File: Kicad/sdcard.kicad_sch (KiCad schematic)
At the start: 4 parts, among them J701 SD_Card

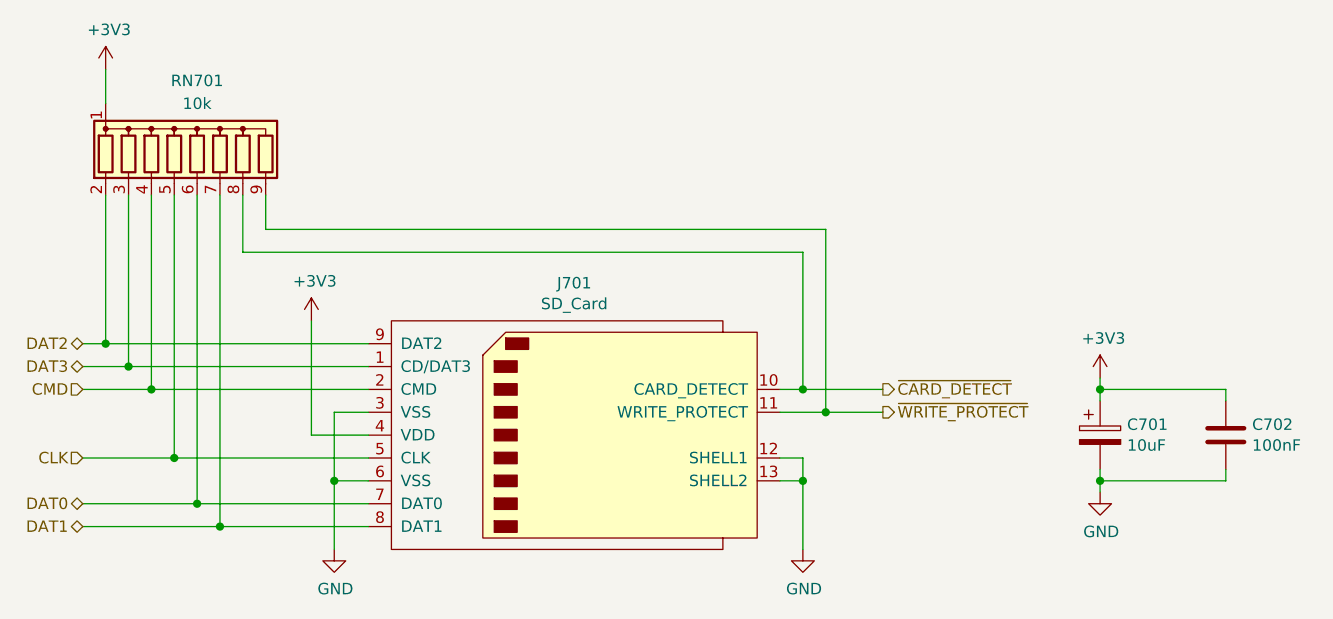
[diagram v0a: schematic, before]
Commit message: Update schematic files to Kicad 6.
Had to fix some symbols which didn't have perfect matches in K6.
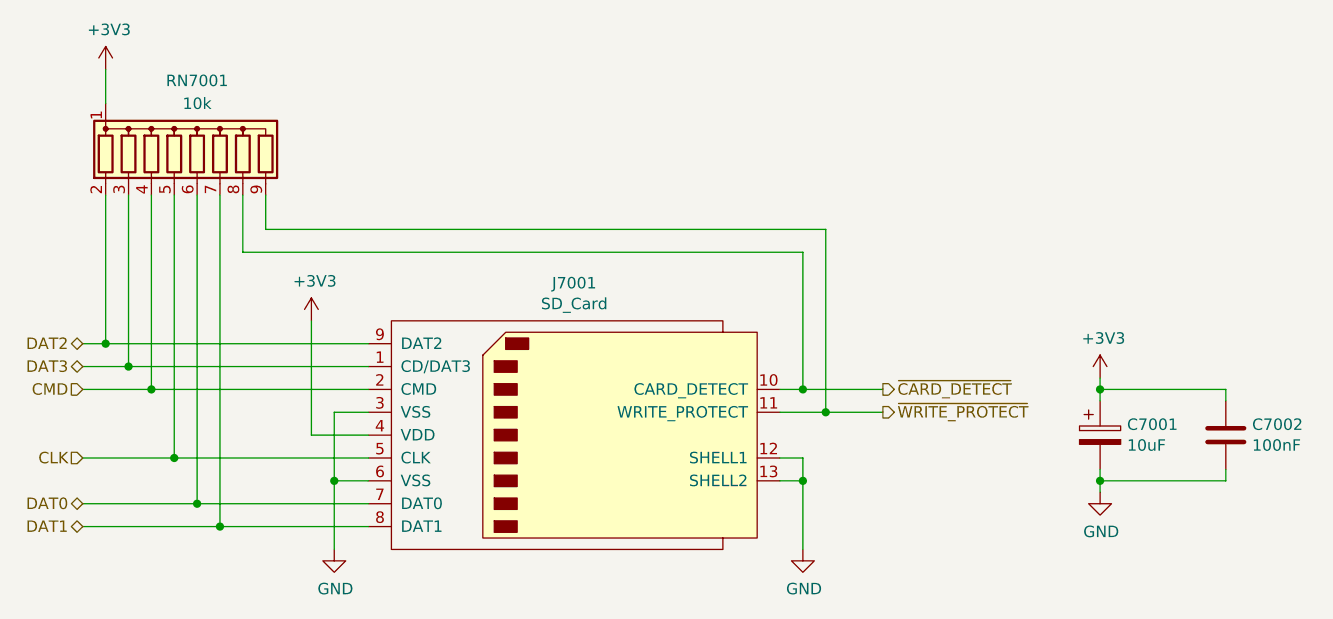
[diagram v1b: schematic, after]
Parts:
- C7001: renamed from C701; symbol Neotron-Common-Hardware-rescue:CP-Device -> Device:C_Polarized
- renumbered C702 to C7002, J701 to J7001, RN701 to RN7001
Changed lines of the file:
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@@
   (symbol (lib_id "Connector:SD_Card") (at 151.13 95.25 0) (unit 1)
     (in_bom yes) (on_board yes)
-    (property "Reference" "J701" (id 0) (at 151.13 78.359 0))
+    (property "Reference" "J7001" (id 0) (at 151.13 78.359 0))
     (property "Value" "SD_Card" (id 1) (at 151.13 80.6704 0))
     (property "Footprint" "Connector_Card:SD_Kyocera_145638009211859+" (id 2) (at 151.13 95.25 0)
@@
   (symbol (lib_id "power:+3V3") (at 121.92 82.55 0) (unit 1)
     (in_bom yes) (on_board yes)
-    (property "Reference" "#PWR0702" (id 0) (at 121.92 86.36 0)
+    (property "Reference" "#PWR07002" (id 0) (at 121.92 86.36 0)
       (effects (font (size 1.27 1.27)) hide)
     )
@@
   (symbol (lib_id "power:GND") (at 124.46 107.95 0) (unit 1)
     (in_bom yes) (on_board yes)
-    (property "Reference" "#PWR0703" (id 0) (at 124.46 114.3 0)
+    (property "Reference" "#PWR07003" (id 0) (at 124.46 114.3 0)
       (effects (font (size 1.27 1.27)) hide)
     )
@@
   (symbol (lib_id "Device:R_Network08") (at 109.22 63.5 0) (unit 1)
     (in_bom yes) (on_board yes)
-    (property "Reference" "RN701" (id 0) (at 109.22 55.88 0))
+    (property "Reference" "RN7001" (id 0) (at 109.22 55.88 0))
     (property "Value" "10k" (id 1) (at 109.22 58.42 0))
     (property "Footprint" "Resistor_THT:R_Array_SIP9" (id 2) (at 118.745 63.5 90)
@@
   (symbol (lib_id "power:+3V3") (at 99.06 54.61 0) (unit 1)
     (in_bom yes) (on_board yes)
-    (property "Reference" "#PWR0701" (id 0) (at 99.06 58.42 0)
+    (property "Reference" "#PWR07001" (id 0) (at 99.06 58.42 0)
       (effects (font (size 1.27 1.27)) hide)
     )
@@
   (symbol (lib_id "power:+3V3") (at 209.55 88.9 0) (unit 1)
     (in_bom yes) (on_board yes)
-    (property "Reference" "#PWR0705" (id 0) (at 209.55 92.71 0)
+    (property "Reference" "#PWR07005" (id 0) (at 209.55 92.71 0)
       (effects (font (size 1.27 1.27)) hide)
     )
@@
   (symbol (lib_id "power:GND") (at 209.55 101.6 0) (unit 1)
     (in_bom yes) (on_board yes)
-    (property "Reference" "#PWR0706" (id 0) (at 209.55 107.95 0)
+    (property "Reference" "#PWR07006" (id 0) (at 209.55 107.95 0)
       (effects (font (size 1.27 1.27)) hide)
     )
@@
     (pin "1")
   )
-  (symbol (lib_id "Neotron-Common-Hardware-rescue:CP-Device") (at 209.55 95.25 0) (unit 1)
-    (in_bom yes) (on_board yes)
-    (property "Reference" "C701" (id 0) (at 212.5472 94.0816 0)
+  (symbol (lib_id "Device:C_Polarized") (at 209.55 95.25 0) (unit 1)
+    (in_bom yes) (on_board yes)
+    (property "Reference" "C7001" (id 0) (at 212.5472 94.0816 0)
       (effects (font (size 1.27 1.27)) (justify left))
     )
@@
   (symbol (lib_id "Device:C") (at 223.52 95.25 0) (unit 1)
     (in_bom yes) (on_board yes)
-    (property "Reference" "C702" (id 0) (at 226.441 94.0816 0)
+    (property "Reference" "C7002" (id 0) (at 226.441 94.0816 0)
       (effects (font (size 1.27 1.27)) (justify left))
     )
@@
   (symbol (lib_id "power:GND") (at 176.53 107.95 0) (unit 1)
     (in_bom yes) (on_board yes)
-    (property "Reference" "#PWR0704" (id 0) (at 176.53 114.3 0)
-      (effects (font (size 1.27 1.27)) hide)
-    )
+    (property "Reference" "#PWR07004" (id 0) (at 176.53 114.3 0)
+      (effects (font (size 1.27 1.27)) hide)
+    )

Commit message: Imported sheets from Neotron Pico.
Standardised on +3V3 not +3.3V
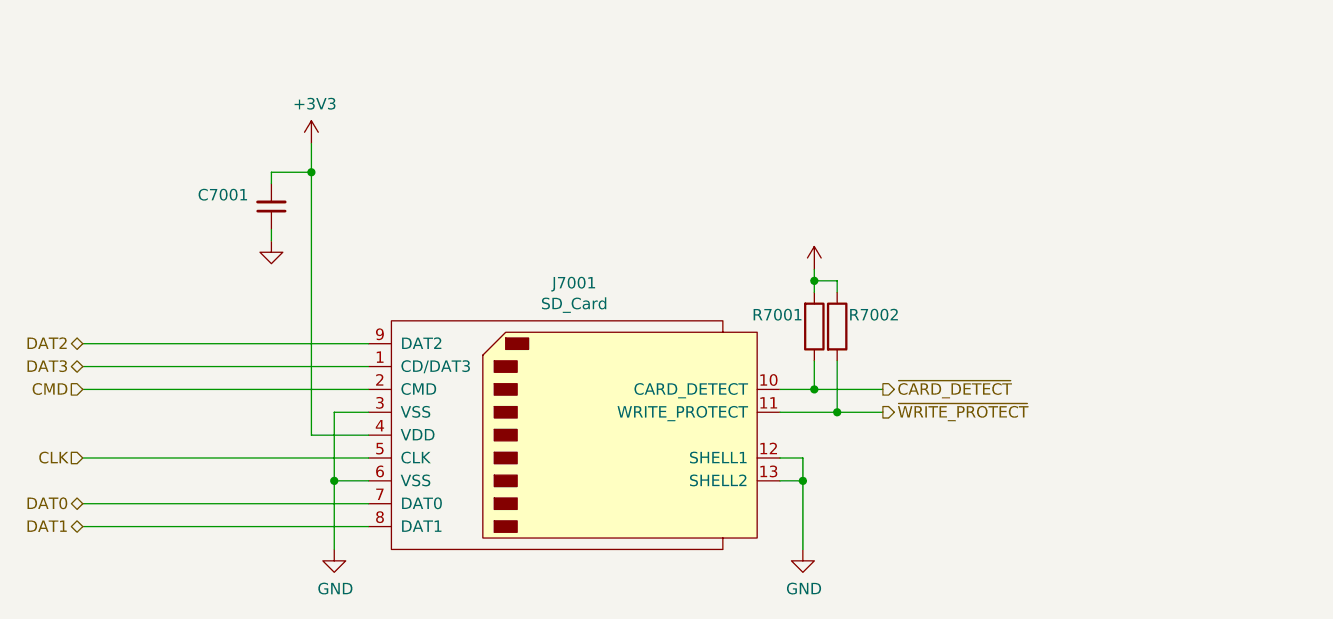
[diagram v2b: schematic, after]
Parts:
- removed C7001: 10uF, Capacitor_SMD:C_0805_2012Metric_Pad1.18x1.45mm_HandSolder, symbol Device:C_Polarized
- removed C7002: 100nF, Capacitor_SMD:C_0805_2012Metric_Pad1.18x1.45mm_HandSolder, symbol Device:C
- removed RN7001: 10k, Resistor_THT:R_Array_SIP9, symbol Device:R_Network08
- added C7001: (no value), symbol Device:C_Small
- added R7001, R7002: (no value), symbol Device:R
- J7001: Digikey 478-4059-1-ND -> 664-GSD090012SEUCT-ND; MPN 145638009211859+ -> GSD090012SEU; Manufacturer Kyocera -> Amphenol; Mouser 581-145638009211859+ -> 523-GSD090012SEU
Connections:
- net +3V3: now also C7001.2, R7001.2, R7002.1
- net GND: now also C7001.1
- net ~{CARD_DETECT}: now also R7001.1
- net ~{WRITE_PROTECT}: now also R7002.2
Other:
- company: https://neotron-compute.github.io/ -> https://neotron-compute.github.io

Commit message: Set missing footprints and update PCB
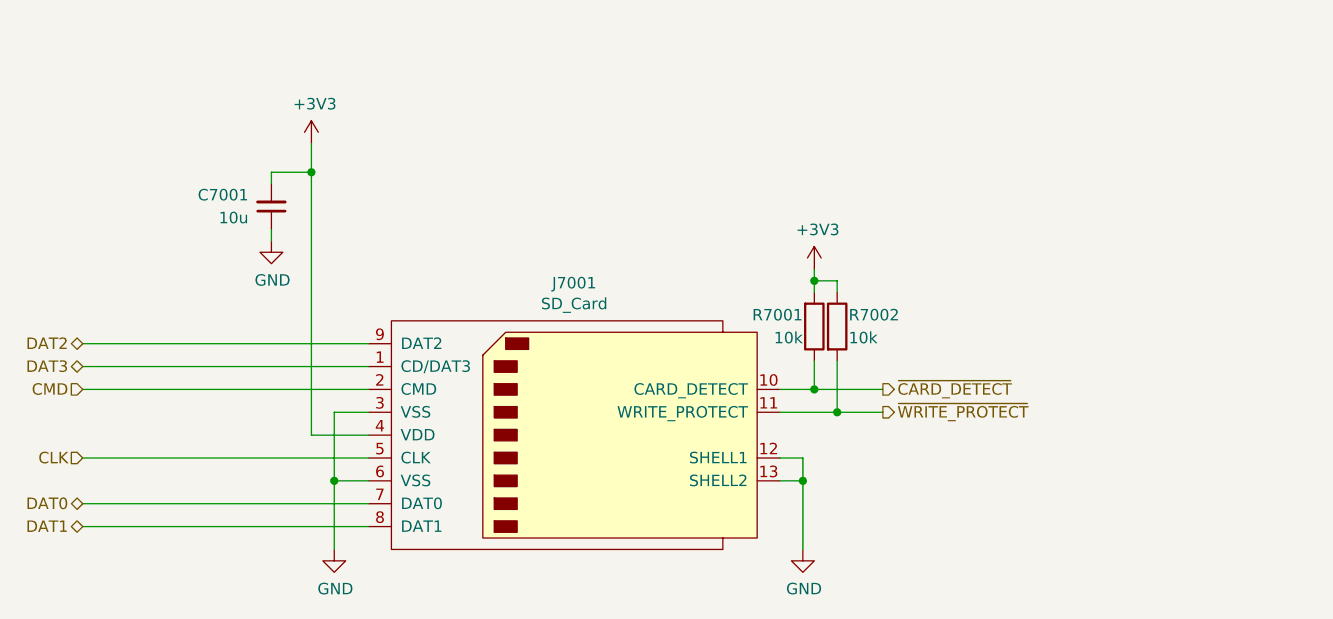
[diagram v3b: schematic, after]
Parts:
- C7001: value (none) -> 10u; footprint (none) -> Capacitor_SMD:C_0805_2012Metric_Pad1.18x1.45mm_HandSolder; JLCPCB Collection Basic -> (none); LCSC Part# C15850 -> (none); MPN CL21A106KAYNNNE -> (none); Manufacturer Samsung -> (none)
- R7001, R7002: value (none) -> 10k; footprint (none) -> Resistor_SMD:R_0805_2012Metric_Pad1.20x1.40mm_HandSolder
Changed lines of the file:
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@@
       (effects (font (size 1.27 1.27)) (justify right))
     )
-    (property "Value" "" (id 1) (at 114.935 71.12 0)
+    (property "Value" "10u" (id 1) (at 114.935 71.12 0)
       (effects (font (size 1.27 1.27)) (justify right))
     )
-    (property "Footprint" "" (id 2) (at 117.475 69.85 0)
+    (property "Footprint" "Capacitor_SMD:C_0805_2012Metric_Pad1.18x1.45mm_HandSolder" (id 2) (at 117.475 69.85 0)
       (effects (font (size 1.27 1.27)) hide)
     )
@@
       (effects (font (size 1.27 1.27)) hide)
     )
-    (property "Digikey" "~" (id 5) (at 117.475 69.85 0)
+    (property "Digikey" "" (id 5) (at 117.475 69.85 0)
       (effects (font (size 1.27 1.27)) hide)
     )
-    (property "MPN" "CL21A106KAYNNNE" (id 6) (at 117.475 69.85 0)
+    (property "MPN" "" (id 6) (at 117.475 69.85 0)
       (effects (font (size 1.27 1.27)) hide)
     )
-    (property "Manufacturer" "Samsung" (id 7) (at 117.475 69.85 0)
+    (property "Manufacturer" "" (id 7) (at 117.475 69.85 0)
       (effects (font (size 1.27 1.27)) hide)
     )
-    (property "LCSC Part#" "C15850" (id 8) (at 117.475 69.85 0)
+    (property "LCSC Part#" "" (id 8) (at 117.475 69.85 0)
       (effects (font (size 1.27 1.27)) hide)
     )
@@
       (effects (font (size 1.27 1.27)) hide)
     )
-    (property "Mouser" "~" (id 11) (at 117.475 69.85 0)
+    (property "Mouser" "" (id 11) (at 117.475 69.85 0)
       (effects (font (size 1.27 1.27)) hide)
     )
-    (property "JLCPCB Collection" "Basic" (id 12) (at 117.475 69.85 0)
+    (property "JLCPCB Collection" "" (id 12) (at 117.475 69.85 0)
       (effects (font (size 1.27 1.27)) hide)
     )
@@
       (effects (font (size 1.27 1.27)) hide)
     )
-    (property "Value" "" (id 1) (at 178.181 72.4408 0))
+    (property "Value" "+3V3" (id 1) (at 178.181 72.4408 0))
     (property "Footprint" "" (id 2) (at 177.8 76.835 0)
       (effects (font (size 1.27 1.27)) hide)
@@
       (effects (font (size 1.27 1.27)) hide)
     )
-    (property "Value" "" (id 1) (at 117.602 78.0542 0))
+    (property "Value" "GND" (id 1) (at 117.602 78.0542 0))
     (property "Footprint" "" (id 2) (at 117.475 73.66 0)
       (effects (font (size 1.27 1.27)) hide)
@@
       (effects (font (size 1.27 1.27)) (justify right))
     )
-    (property "Value" "" (id 1) (at 176.53 84.455 0)
+    (property "Value" "10k" (id 1) (at 176.53 84.455 0)
       (effects (font (size 1.27 1.27)) (justify right))
     )
-    (property "Footprint" "" (id 2) (at 176.022 83.185 90)
+    (property "Footprint" "Resistor_SMD:R_0805_2012Metric_Pad1.20x1.40mm_HandSolder" (id 2) (at 176.022 83.185 90)
       (effects (font (size 1.27 1.27)) hide)
     )
@@
       (effects (font (size 1.27 1.27)) (justify left))
     )
-    (property "Value" "" (id 1) (at 181.61 84.455 0)
+    (property "Value" "10k" (id 1) (at 181.61 84.455 0)
       (effects (font (size 1.27 1.27)) (justify left))
     )
-    (property "Footprint" "" (id 2) (at 178.562 83.185 90)
+    (property "Footprint" "Resistor_SMD:R_0805_2012Metric_Pad1.20x1.40mm_HandSolder" (id 2) (at 178.562 83.185 90)
       (effects (font (size 1.27 1.27)) hide)
     )

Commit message: Re-imported from Neotron Pico v1.1.
This time I deleted the sheets from the top level and then re-added pointing at the new files. I also reset the PCB dimensions to match the Neotron Pico.

This seems to have done a better job importing footprints.
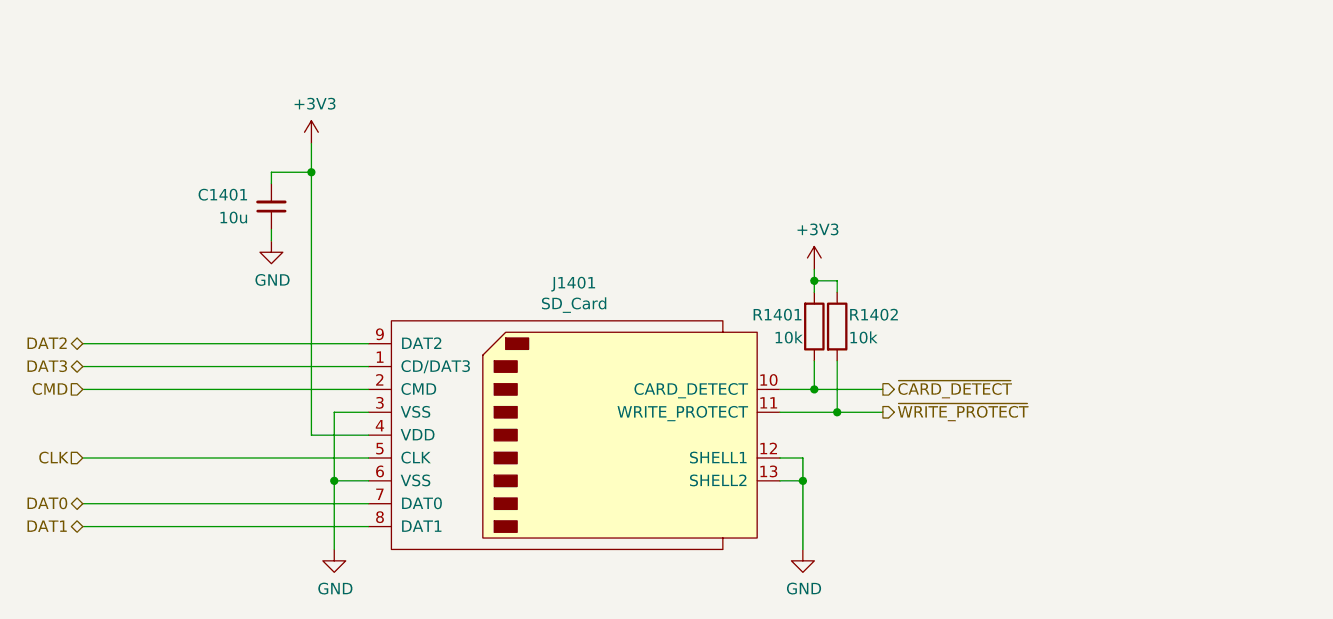
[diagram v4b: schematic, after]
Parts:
- C1401: renamed from C7001; JLCPCB Collection (none) -> Basic; LCSC Part# (none) -> C15850; MPN (none) -> CL21A106KAYNNNE; Manufacturer (none) -> Samsung
- J1401: renamed from J7001; footprint Connector_Card:SD_Kyocera_145638009211859+ -> Neotron-Common-Hardware:Amphenol_GSD090012SEU
- renumbered R7001 to R1401, R7002 to R1402
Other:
- company: https://neotron-compute.github.io -> https://neotron-compute.github.io/
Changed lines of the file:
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@@
     (title "Neotron Common Hardware - SD Card Slot")
     (date "${date}")
-    (rev "${version}")
-    (company "https://neotron-compute.github.io")
-    (comment 1 "Licensed as CC-BY-SA")
+    (rev "[Uncontrolled]")
+    (company "https://neotron-compute.github.io/")
+    (comment 1 "Licenced as CC BY-SA")
     (comment 2 "Copyright (c) The Neotron Developers, 2022")
   )
@@
   (symbol (lib_id "Connector:SD_Card") (at 151.13 95.25 0) (unit 1)
     (in_bom yes) (on_board yes)
-    (property "Reference" "J7001" (id 0) (at 151.13 78.359 0))
+    (property "Reference" "J1401" (id 0) (at 151.13 78.359 0))
     (property "Value" "SD_Card" (id 1) (at 151.13 80.6704 0))
-    (property "Footprint" "Connector_Card:SD_Kyocera_145638009211859+" (id 2) (at 151.13 95.25 0)
+    (property "Footprint" "Neotron-Common-Hardware:Amphenol_GSD090012SEU" (id 2) (at 151.13 95.25 0)
       (effects (font (size 1.27 1.27)) hide)
     )
@@
   (symbol (lib_id "power:+3V3") (at 121.92 62.865 0) (unit 1)
     (in_bom yes) (on_board yes)
-    (property "Reference" "#PWR07002" (id 0) (at 121.92 66.675 0)
+    (property "Reference" "#PWR01402" (id 0) (at 121.92 66.675 0)
       (effects (font (size 1.27 1.27)) hide)
     )
@@
   (symbol (lib_id "power:GND") (at 124.46 107.95 0) (unit 1)
     (in_bom yes) (on_board yes)
-    (property "Reference" "#PWR07003" (id 0) (at 124.46 114.3 0)
+    (property "Reference" "#PWR01403" (id 0) (at 124.46 114.3 0)
       (effects (font (size 1.27 1.27)) hide)
     )
@@
   (symbol (lib_id "power:GND") (at 176.53 107.95 0) (unit 1)
     (in_bom yes) (on_board yes)
-    (property "Reference" "#PWR07004" (id 0) (at 176.53 114.3 0)
+    (property "Reference" "#PWR01404" (id 0) (at 176.53 114.3 0)
       (effects (font (size 1.27 1.27)) hide)
     )
@@
   (symbol (lib_id "Device:C_Small") (at 117.475 69.85 0) (mirror x) (unit 1)
     (in_bom yes) (on_board yes)
-    (property "Reference" "C7001" (id 0) (at 114.935 68.58 0)
+    (property "Reference" "C1401" (id 0) (at 114.935 68.58 0)
       (effects (font (size 1.27 1.27)) (justify right))
     )
@@
       (effects (font (size 1.27 1.27)) hide)
     )
-    (property "Digikey" "" (id 5) (at 117.475 69.85 0)
-      (effects (font (size 1.27 1.27)) hide)
-    )
-    (property "MPN" "" (id 6) (at 117.475 69.85 0)
-      (effects (font (size 1.27 1.27)) hide)
-    )
-    (property "Manufacturer" "" (id 7) (at 117.475 69.85 0)
-      (effects (font (size 1.27 1.27)) hide)
-    )
-    (property "LCSC Part#" "" (id 8) (at 117.475 69.85 0)
+    (property "Digikey" "~" (id 5) (at 117.475 69.85 0)
+      (effects (font (size 1.27 1.27)) hide)
+    )
+    (property "MPN" "CL21A106KAYNNNE" (id 6) (at 117.475 69.85 0)
+      (effects (font (size 1.27 1.27)) hide)
+    )
+    (property "Manufacturer" "Samsung" (id 7) (at 117.475 69.85 0)
+      (effects (font (size 1.27 1.27)) hide)
+    )
+    (property "LCSC Part#" "C15850" (id 8) (at 117.475 69.85 0)
       (effects (font (size 1.27 1.27)) hide)
     )
@@
       (effects (font (size 1.27 1.27)) hide)
     )
-    (property "Mouser" "" (id 11) (at 117.475 69.85 0)
-      (effects (font (size 1.27 1.27)) hide)
-    )
-    (property "JLCPCB Collection" "" (id 12) (at 117.475 69.85 0)
+    (property "Mouser" "~" (id 11) (at 117.475 69.85 0)
+      (effects (font (size 1.27 1.27)) hide)
+    )
+    (property "JLCPCB Collection" "Basic" (id 12) (at 117.475 69.85 0)
       (effects (font (size 1.27 1.27)) hide)
     )
@@
   (symbol (lib_id "power:+3V3") (at 177.8 76.835 0) (unit 1)
     (in_bom yes) (on_board yes)
-    (property "Reference" "#PWR07005" (id 0) (at 177.8 80.645 0)
+    (property "Reference" "#PWR01405" (id 0) (at 177.8 80.645 0)
       (effects (font (size 1.27 1.27)) hide)
     )
@@
   (symbol (lib_id "power:GND") (at 117.475 73.66 0) (unit 1)
     (in_bom yes) (on_board yes)
-    (property "Reference" "#PWR07001" (id 0) (at 117.475 80.01 0)
+    (property "Reference" "#PWR01401" (id 0) (at 117.475 80.01 0)
       (effects (font (size 1.27 1.27)) hide)
     )
@@
   (symbol (lib_id "Device:R") (at 177.8 83.185 0) (mirror x) (unit 1)
     (in_bom yes) (on_board yes)
-    (property "Reference" "R7001" (id 0) (at 176.53 81.915 0)
+    (property "Reference" "R1401" (id 0) (at 176.53 81.915 0)
       (effects (font (size 1.27 1.27)) (justify right))
     )
@@
   (symbol (lib_id "Device:R") (at 180.34 83.185 0) (unit 1)
     (in_bom yes) (on_board yes)
-    (property "Reference" "R7002" (id 0) (at 181.61 81.915 0)
+    (property "Reference" "R1402" (id 0) (at 181.61 81.915 0)
       (effects (font (size 1.27 1.27)) (justify left))
     )
